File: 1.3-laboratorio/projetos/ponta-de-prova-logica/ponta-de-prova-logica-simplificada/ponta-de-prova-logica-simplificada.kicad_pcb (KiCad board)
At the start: 2 copper layers, 64.8 x 40 mm, 21 parts, among them J1 Conn_01x02, J2 PONTA DE PROVA, SW1 SW_DPDT_x2, U1 LM339

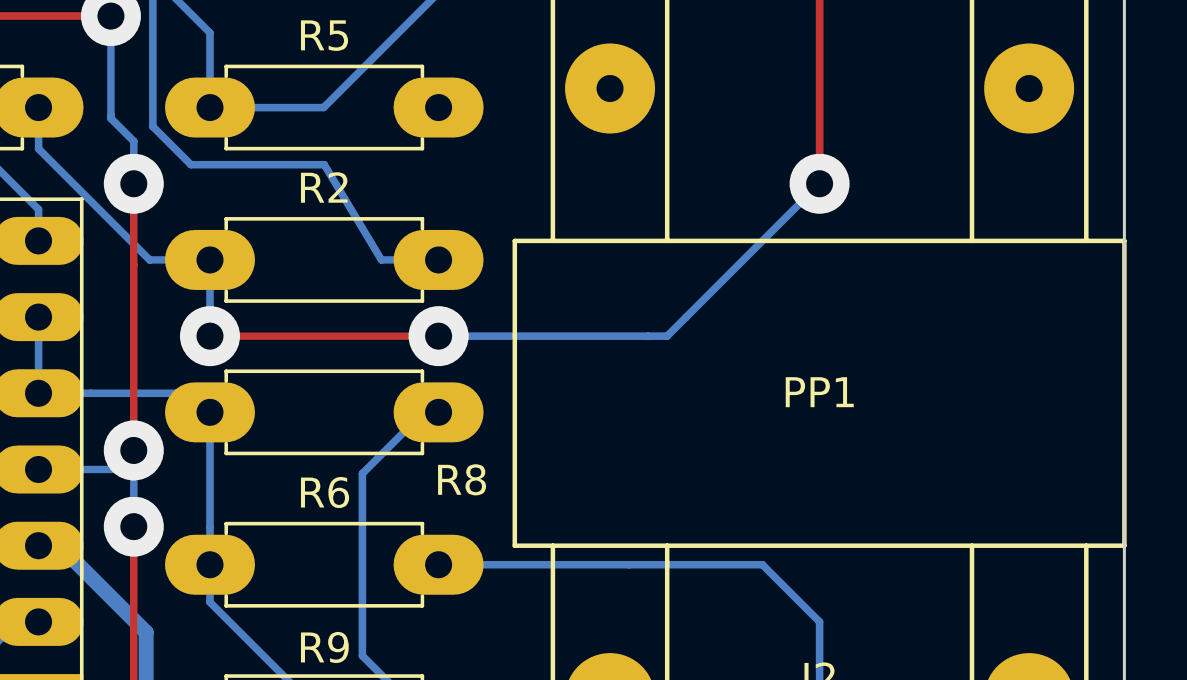
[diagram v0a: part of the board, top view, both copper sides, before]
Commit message: Remoção de um 'jumper' e inclusão de identificação da placa na camada de cobre de baixo.
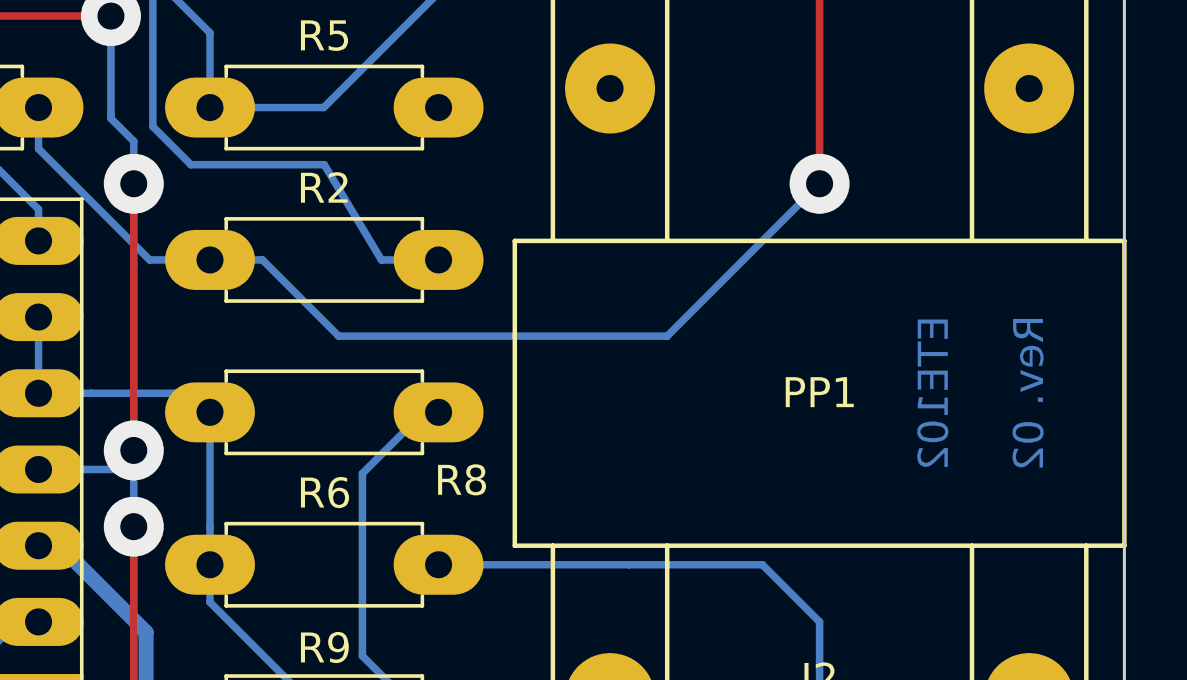
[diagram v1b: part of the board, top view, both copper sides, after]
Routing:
- net Net-(R1-Pad2): track 103.5 -> 102.0 mm, vias 4 -> 2
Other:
- board text added: "ETE102"
- board text added: "Rev. 02"
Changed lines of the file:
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@@
   (general
     (thickness 1.6)
-    (drawings 12)
-    (tracks 178)
+    (drawings 14)
+    (tracks 173)
     (zones 0)
     (modules 21)
@@
     (visible_elements 7FFFFFFF)
     (pcbplotparams
-      (layerselection 0x010fc_ffffffff)
+      (layerselection 0x00000_fffffffe)
       (usegerberextensions false)
       (usegerberattributes false)
@@
       (hpglpenspeed 20)
       (hpglpendiameter 15.000000)
-      (psnegative false)
+      (psnegative true)
       (psa4output false)
-      (plotreference true)
-      (plotvalue true)
+      (plotreference false)
+      (plotvalue false)
       (plotinvisibletext false)
       (padsonsilk false)
       (subtractmaskfromsilk false)
-      (outputformat 1)
-      (mirror false)
-      (drillshape 0)
+      (outputformat 4)
+      (mirror true)
+      (drillshape 2)
       (scaleselection 1)
       (outputdirectory "gerber/"))
@@
     )
   )
+  (gr_text ETE102 (at 181.61 99.695 90) (layer B.Cu)
+    (effects (font (size 1 1) (thickness 0.2)) (justify mirror))
+  )
+  (gr_text "Rev. 02" (at 184.785 99.695 90) (layer B.Cu)
+    (effects (font (size 1 1) (thickness 0.2)) (justify mirror))
+  )
   (gr_arc (start 125.73 116.84) (end 123.19 116.84) (angle -90) (layer Edge.Cuts) (width 0.1))
   (gr_arc (start 185.42 116.84) (end 185.42 119.38) (angle -90) (layer Edge.Cuts) (width 0.1))
@@
   (segment (start 127.635 109.855) (end 128.135 109.855) (width 0.25) (layer B.Cu) (net 4))
   (segment (start 131.945 113.665) (end 134.62 113.665) (width 0.25) (layer B.Cu) (net 4))
-  (via (at 165.1 97.79) (size 2) (drill 0.9) (layers F.Cu B.Cu) (net 5))
-  (segment (start 157.48 97.79) (end 157.48 95.885) (width 0.25) (layer B.Cu) (net 5))
-  (segment (start 157.48 95.885) (end 157.48 95.25) (width 0.25) (layer B.Cu) (net 5))
-  (segment (start 165.1 97.79) (end 157.48 97.79) (width 0.25) (layer F.Cu) (net 5))
-  (via (at 157.48 97.79) (size 2) (drill 0.9) (layers F.Cu B.Cu) (net 5))
-  (segment (start 172.085 97.79) (end 165.1 97.79) (width 0.25) (layer B.Cu) (net 5))
-  (segment (start 173.355 97.155) (end 172.72 97.79) (width 0.25) (layer B.Cu) (net 5))
-  (segment (start 172.72 97.79) (end 172.085 97.79) (width 0.25) (layer B.Cu) (net 5))
   (via (at 177.8 85.09) (size 2) (drill 0.9) (layers F.Cu B.Cu) (net 5))
   (via (at 177.8 92.71) (size 2) (drill 0.9) (layers F.Cu B.Cu) (net 5))
   (segment (start 177.8 85.09) (end 177.8 92.71) (width 0.25) (layer F.Cu) (net 5))
-  (segment (start 177.8 92.71) (end 173.355 97.155) (width 0.25) (layer B.Cu) (net 5))
   (segment (start 155.469999 95.25) (end 157.48 95.25) (width 0.25) (layer B.Cu) (net 5))
   (segment (start 151.765 90.17) (end 151.765 91.545001) (width 0.25) (layer B.Cu) (net 5))
@@
   (segment (start 128.13501 81.41499) (end 137.29499 81.41499) (width 0.25) (layer B.Cu) (net 5))
   (segment (start 137.29499 81.41499) (end 137.795 81.915) (width 0.25) (layer B.Cu) (net 5))
+  (segment (start 159.23 95.25) (end 157.48 95.25) (width 0.25) (layer B.Cu) (net 5))
+  (segment (start 161.77 97.79) (end 159.23 95.25) (width 0.25) (layer B.Cu) (net 5))
+  (segment (start 172.72 97.79) (end 161.77 97.79) (width 0.25) (layer B.Cu) (net 5))
+  (segment (start 177.8 92.71) (end 172.72 97.79) (width 0.25) (layer B.Cu) (net 5))
   (segment (start 157.48 83.185) (end 157.48 85.09) (width 0.25) (layer B.Cu) (net 6))
   (segment (start 156.845 82.55) (end 157.48 83.185) (width 0.25) (layer B.Cu) (net 6))

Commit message: Arquivos PDF para confecção da placa.
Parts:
- D1: value LED ALTO -> ALTO
- D2: value LED BAIXO -> BAIXO
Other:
- board text added: "2x 820/0.5W"

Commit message: Arquivos para impressão de fotolito preparados.
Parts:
- moved C1 127.0 mm to (31.1, 29.8)
- moved C2 127.0 mm to (31.1, 43.8)
- moved D1 127.0 mm to (19.1, 48.9)
- moved J2 127.0 mm to (68.6, 46.4)
- moved R1 127.0 mm to (34.9, 25.4)
- moved D2 127.0 mm to (25.4, 48.9)
- moved J1 127.0 mm to (22.2, 35.6)
- moved R11 127.0 mm to (18.4, 41.3)
- moved R12 127.0 mm to (18.4, 45.1)
- moved R2 127.0 mm to (48.3, 30.5)
- moved R4 127.0 mm to (48.3, 20.3)
- moved R5 127.0 mm to (48.3, 25.4)
- moved R6 127.0 mm to (48.3, 40.6)
- moved R7 127.0 mm to (48.3, 50.8)
- moved R8 127.0 mm to (48.3, 35.6)
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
